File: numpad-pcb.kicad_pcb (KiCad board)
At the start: 2 copper layers, 62 parts, among them J1 AVR-ISP-6, SW1 SW_Push, SW10 7/home, SW11 8/up, SW12 9/pgup, SW13 +, SW14 4/left, SW15 5, SW16 6/right, SW18 1/end, SW19 2/down, SW2 ESC, SW20 3/pgdn, SW22 0/insert, SW23 ./delete, SW24 ENTER, SW3 TAB, SW4 BACKSPACE, SW5 FN, SW6 NUM_LOCK, SW7 /, SW8 *, SW9 -, U1 ATmega32U4-A, Y1 Crystal_GND24_Small

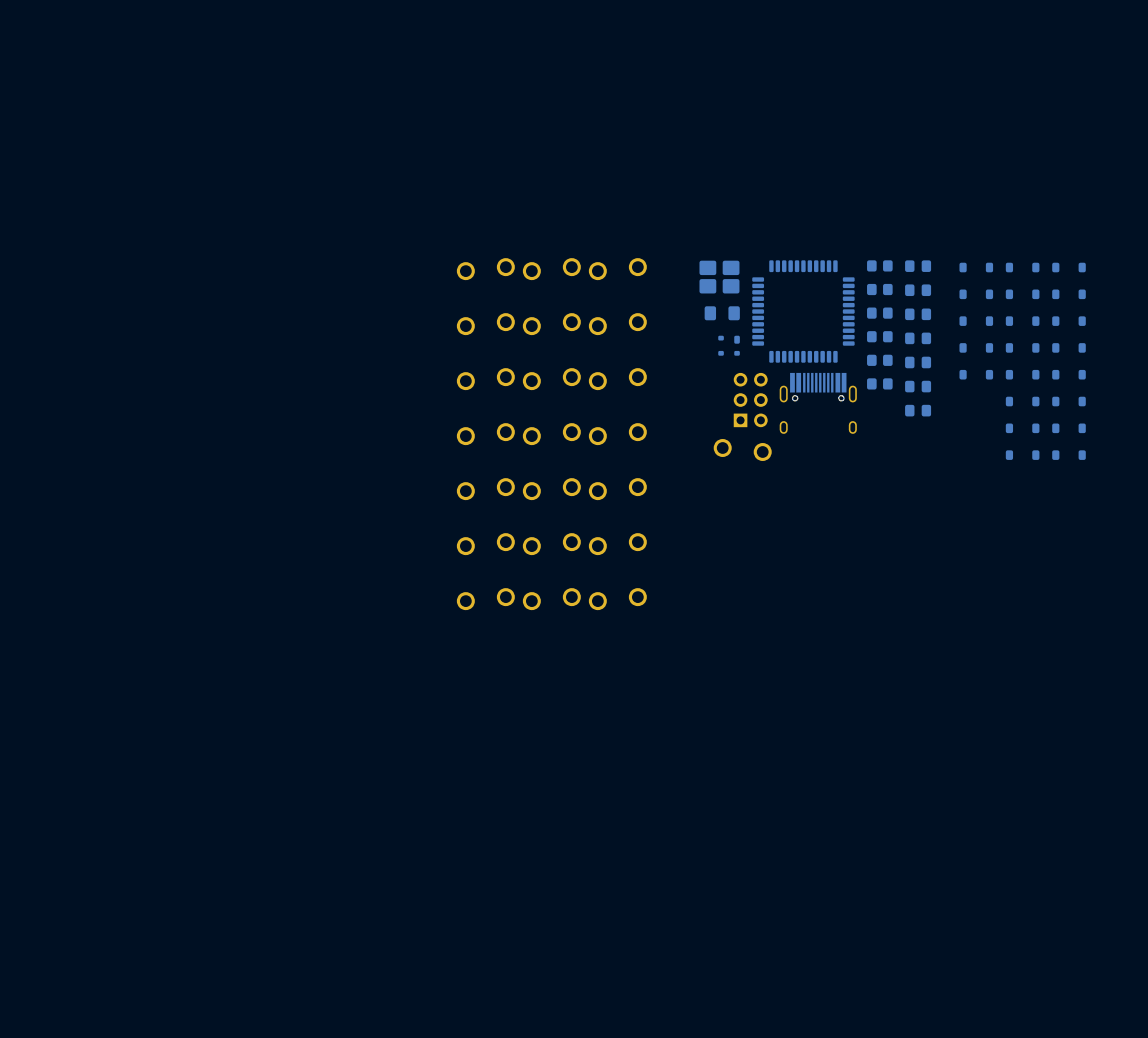
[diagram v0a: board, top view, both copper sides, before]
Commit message: Correct PCB footprints
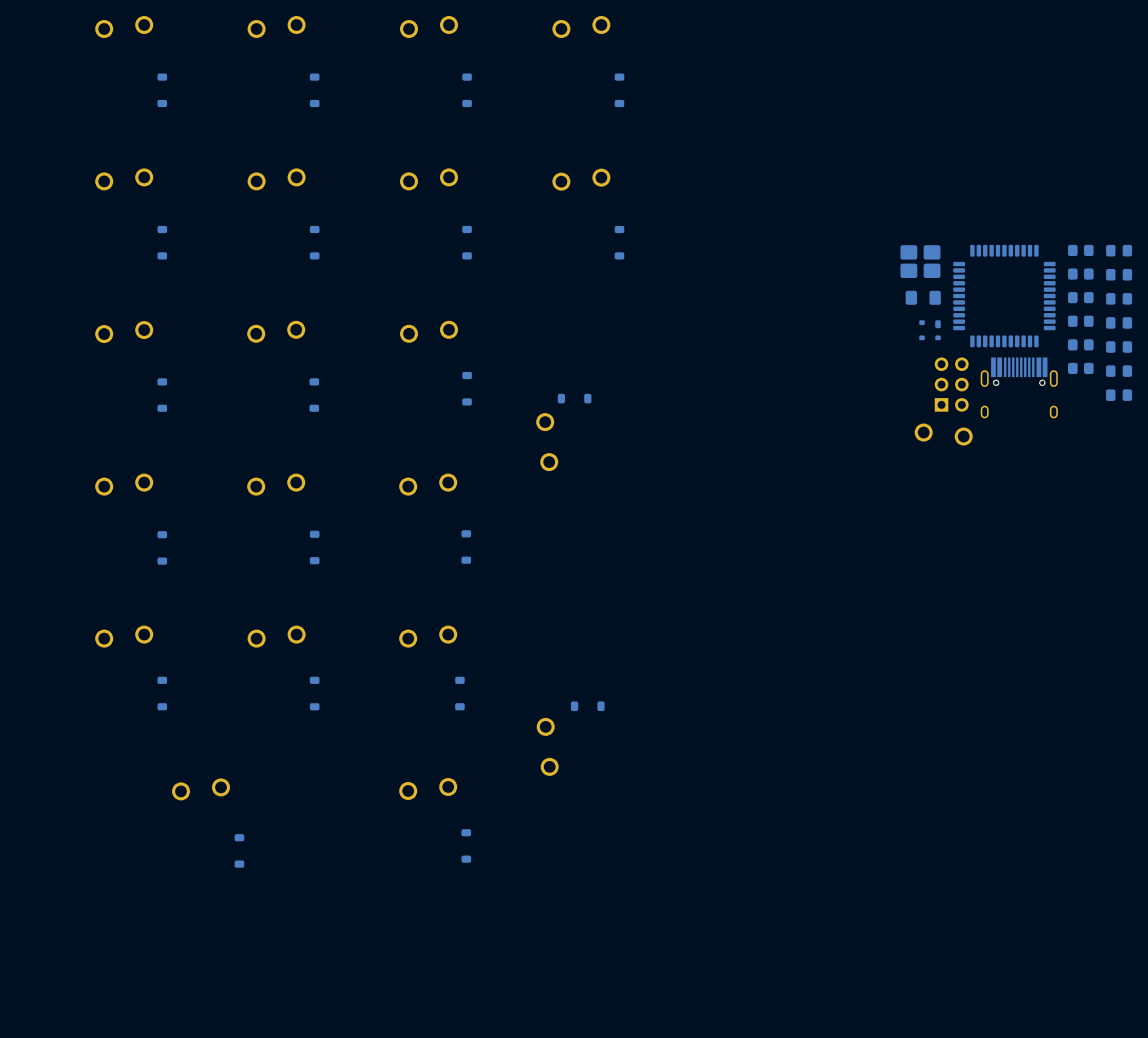
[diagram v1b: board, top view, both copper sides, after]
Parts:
- SW11: value 8/up -> 4/left
- SW12: value 9/pgup -> 8/up
- SW13: value + -> 5; footprint Alps_Only:ALPS-2U -> Alps_Only:ALPS-1U
- SW14: value 4/left -> 9/pgup
- SW15: value 5 -> 6/right
- SW16: value 6/right -> +; footprint Alps_Only:ALPS-1U -> Alps_Only:ALPS-2U
- SW19: value 2/down -> 0/insert; footprint Alps_Only:ALPS-1U -> Alps_Only:ALPS-2U
- SW20: value 3/pgdn -> 2/down
- SW22: value 0/insert -> 3/pgdn; footprint Alps_Only:ALPS-2U -> Alps_Only:ALPS-1U
- moved D19 117.5 mm to (77.9, 137.9), turned to 90 degrees
- moved D2 115.5 mm to (68.3, 42.9), turned to 90 degrees
- moved D6 114.5 mm to (68.3, 61.9), turned to 90 degrees
- moved D11 112.1 mm to (68.3, 100.1), turned to 90 degrees
- moved D18 111.6 mm to (68.3, 118.3), turned to 90 degrees
- moved D10 108.7 mm to (68.3, 81.0), turned to 90 degrees
- moved D3 97.7 mm to (87.3, 42.9), turned to 90 degrees
- moved D20 96.6 mm to (87.3, 118.3), turned to 90 degrees
- moved D7 96.4 mm to (87.3, 61.9), turned to 90 degrees
- moved D13 91.9 mm to (87.3, 100.0), turned to 90 degrees
- moved D23 89.1 mm to (106.3, 137.3), turned to 90 degrees
- moved D12 89.0 mm to (87.3, 81.0), turned to 90 degrees
- moved D4 80.6 mm to (106.4, 42.9), turned to 90 degrees
- moved D22 79.6 mm to (105.5, 118.3), turned to 90 degrees
- moved D8 78.7 mm to (106.4, 61.9), turned to 90 degrees
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
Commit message: Initial layout of PCB components
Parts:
- moved R6 102.3 mm to (84.1, 51.8)
- moved R1 99.1 mm to (112.1, 132.0)
- moved C3 98.8 mm to (108.7, 128.0), turned to 90 degrees
- moved USB1 98.7 mm to (88.0, 39.6), turned to 0 degrees
- moved C1 95.8 mm to (121.4, 132.0)
- moved R5 94.6 mm to (91.2, 51.8)
- moved C4 87.3 mm to (109.5, 110.5)
- moved R3 83.8 mm to (112.7, 114.3), turned to -90 degrees
- moved R2 83.5 mm to (115.1, 114.3), turned to -90 degrees
- moved C2 83.3 mm to (124.6, 120.1), turned to -90 degrees
- moved F1 80.8 mm to (83.3, 58.2), turned to -90 degrees
- moved C5 79.5 mm to (119.4, 115.3)
- moved U1 79.0 mm to (116.7, 123.4), turned to -90 degrees
- moved D1 77.7 mm to (88.1, 57.4)
- moved SW1 77.5 mm to (116.5, 149.8)
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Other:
- board outline added: 76.2 x 118.3 mm

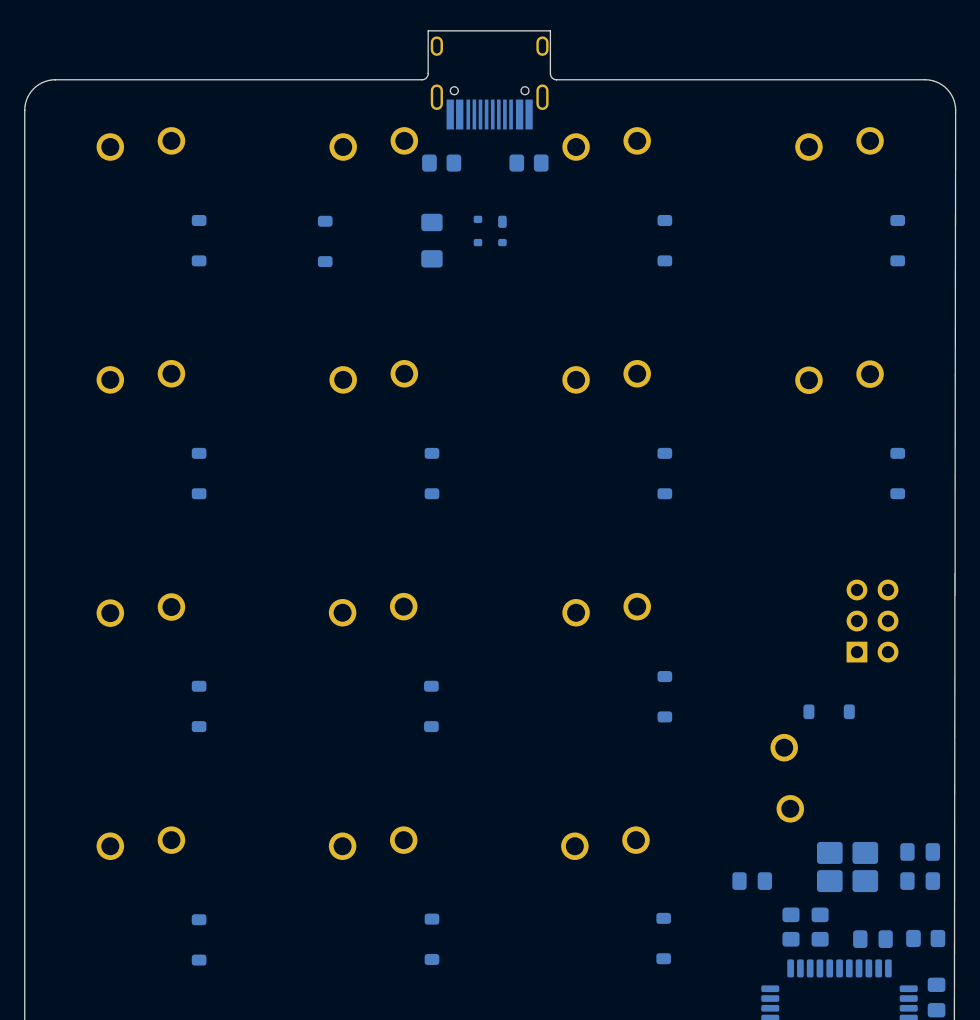
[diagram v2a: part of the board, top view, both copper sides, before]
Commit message: Fix silkscreen errors
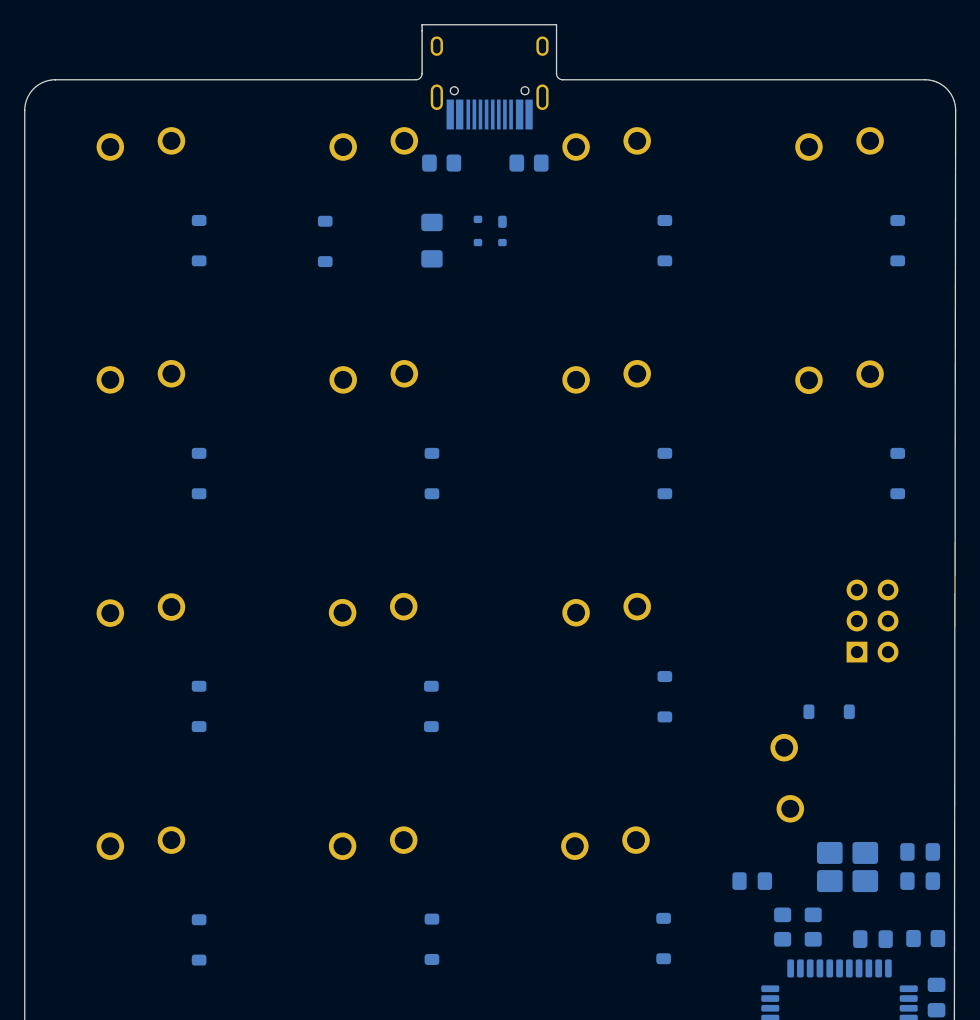
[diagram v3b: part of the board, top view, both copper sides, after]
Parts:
- moved R3 0.68 mm to (112.0, 114.3)
- moved R2 0.56 mm to (114.5, 114.3)
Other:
- board size 76.2 x 118.3 mm -> 76.2 x 118.8 mm
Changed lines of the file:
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@@
 		(tags "capacitor handsolder")
 		(property "Reference" "C7"
-			(at 0 1.68 0)
+			(at 0 -1.95 0)
 			(layer "B.SilkS")
 			(effects
@@
 		(tags "resistor handsolder")
 		(property "Reference" "R1"
-			(at 0 1.65 0)
+			(at 1.09375 1.65 0)
 			(layer "B.SilkS")
 			(effects
@@
 	(footprint "Resistor_SMD:R_0805_2012Metric_Pad1.20x1.40mm_HandSolder"
 		(layer "B.Cu")
-		(at 112.68125 114.3125 -90)
+		(at 112 114.3125 -90)
 		(descr "Resistor SMD 0805 (2012 Metric), square (rectangular) end terminal, IPC-7351 nominal with elongated pad for handsoldering. (Body size source: IPC-SM-782 page 72, https://www.pcb-3d.com/wordpress/wp-content/uploads/ipc-sm-782a_amendment_1_and_2.pdf), generated with kicad-footprint-generator")
 		(tags "resistor handsolder")
@@
 		(tags "capacitor handsolder")
 		(property "Reference" "C3"
-			(at 0 1.68 90)
+			(at -2.9875 -0.2125 90)
 			(layer "B.SilkS")
 			(effects
@@
 	(footprint "Resistor_SMD:R_0805_2012Metric_Pad1.20x1.40mm_HandSolder"
 		(layer "B.Cu")
-		(at 115.0625 114.3125 -90)
+		(at 114.5 114.3125 -90)
 		(descr "Resistor SMD 0805 (2012 Metric), square (rectangular) end terminal, IPC-7351 nominal with elongated pad for handsoldering. (Body size source: IPC-SM-782 page 72, https://www.pcb-3d.com/wordpress/wp-content/uploads/ipc-sm-782a_amendment_1_and_2.pdf), generated with kicad-footprint-generator")
 		(tags "resistor handsolder")
 		(property "Reference" "R2"
-			(at 0 1.65 90)
+			(at 0.1875 -1.9375 90)
 			(layer "B.SilkS")
 			(effects
@@
 	)
 	(gr_arc
-		(start 83 44.5)
-		(mid 82.853553 44.853553)
-		(end 82.5 45)
+		(start 82.5 44.5)
+		(mid 82.353553 44.853553)
+		(end 82 45)
 		(stroke
 			(width 0.05)
@@
 	)
 	(gr_line
-		(start 82.5 45)
-		(end 52.5 45)
+		(start 82.5 40.5)
+		(end 93.5 40.5)
 		(stroke
 			(width 0.05)
@@
 	)
 	(gr_line
-		(start 83 41)
-		(end 93 41)
+		(start 126 156.8)
+		(end 126.15 47.5)
+		(stroke
+			(width 0.05)
+			(type default)
+		)
+		(layer "Edge.Cuts")
+	)
+	(gr_arc
+		(start 52.5 159.3)
+		(mid 50.732233 158.567767)
+		(end 50 156.8)
 		(stroke
 			(width 0.05)
@@
 	)
 	(gr_line
-		(start 126 156.8)
-		(end 126.15 47.5)
+		(start 82.5 41)
+		(end 82.5 40.5)
 		(stroke
 			(width 0.05)
@@
 		(layer "Edge.Cuts")
 	)
-	(gr_arc
-		(start 52.5 159.3)
-		(mid 50.732233 158.567767)
-		(end 50 156.8)
+	(gr_line
+		(start 93.5 41)
+		(end 93.5 40.5)
 		(stroke
 			(width 0.05)
@@
 		(layer "Edge.Cuts")
 	)
+	(gr_line
+		(start 94 45)
+		(end 123.65 45)
+		(stroke
+			(width 0.05)
+			(type default)
+		)
+		(layer "Edge.Cuts")
+	)
 	(gr_arc
 		(start 123.65 45)
@@
 	)
 	(gr_line
-		(start 93 41)
-		(end 93 44.5)
+		(start 93.5 41)
+		(end 93.5 44.5)
 		(stroke
 			(width 0.05)
 			(type default)
 		)
+		(locked yes)
 		(layer "Edge.Cuts")
 	)
-	(gr_arc
-		(start 93.5 45)
-		(mid 93.146447 44.853553)
-		(end 93 44.5)
+	(gr_line
+		(start 52.5 45)
+		(end 82 45)
 		(stroke
 			(width 0.05)
@@
 		(layer "Edge.Cuts")
 	)
-	(gr_line
-		(start 83 44.5)
-		(end 83 41)
+	(gr_arc
+		(start 94 45)
+		(mid 93.646447 44.853553)
+		(end 93.5 44.5)
 		(stroke
 			(width 0.05)
 			(type default)
 		)
+		(locked yes)
 		(layer "Edge.Cuts")
 	)
 	(gr_line
-		(start 123.65 45)
-		(end 93.5 45)
+		(start 82.5 44.5)
+		(end 82.5 41)
 		(stroke
 			(width 0.05)
